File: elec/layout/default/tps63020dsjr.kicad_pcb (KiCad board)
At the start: 2 copper layers, 225.7 x 100.8 mm, 0 parts

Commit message: layout
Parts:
- added C1: Multilayer Ceramic Capacitors MLCC - SMD/SMT 10uF 10V 0805 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, lib:C0805, F.Cu at (118.5, 46.4)
- added C2: Multilayer Ceramic Capacitors MLCC - SMD/SMT 10uF 10V 0805 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, lib:C0805, F.Cu at (118.5, 44.4)
- added C3: Multilayer Ceramic Capacitors MLCC - SMD/SMT 10uF 10V 0805 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, lib:C0805, F.Cu at (118.4, 53.6)
- added C4: Multilayer Ceramic Capacitors MLCC - SMD/SMT 10uF 10V 0805 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, lib:C0805, F.Cu at (118.4, 55.6)
- added C5: Multilayer Ceramic Capacitors MLCC - SMD/SMT 100nF 10V 0402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, lib:C0402, F.Cu at (115.6, 51.1)
- added L1: , lib:IND-SMD_L2.5-W2.0_WPN252012H, F.Cu at (122.7, 49.6)
- added R1: Chip Resistor - Surface Mount 1MOhms ±5% 1/16W 0402 RoHS, lib:R0402, F.Cu at (119.1, 52.1)
- added R2: Chip Resistor - Surface Mount 180KOhms ±5% 1/16W 0402 RoHS, lib:R0402, F.Cu at (117.2, 52.1)
- added R3: Chip Resistor - Surface Mount 1MOhms ±5% 1/16W 0402 RoHS, lib:R0402, F.Cu at (115.7, 48.1)
- added U1: , lib:VSON-14_L4.0-W3.0-P0.50-BL-EP_TI_DSJ, F.Cu at (119.0, 49.5)
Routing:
- net vcc-1: track 0.00 -> 6.20 mm
- net vcc: track 0.00 -> 5.63 mm
- net l1: track 0.00 -> 2.59 mm
- net l2: track 0.00 -> 2.54 mm
- net out: track 0.00 -> 2.08 mm
- net gnd: track 0.00 -> 1.99 mm
- net vina: track 0.00 -> 1.41 mm
- net pg: track 0.00 -> 1.29 mm

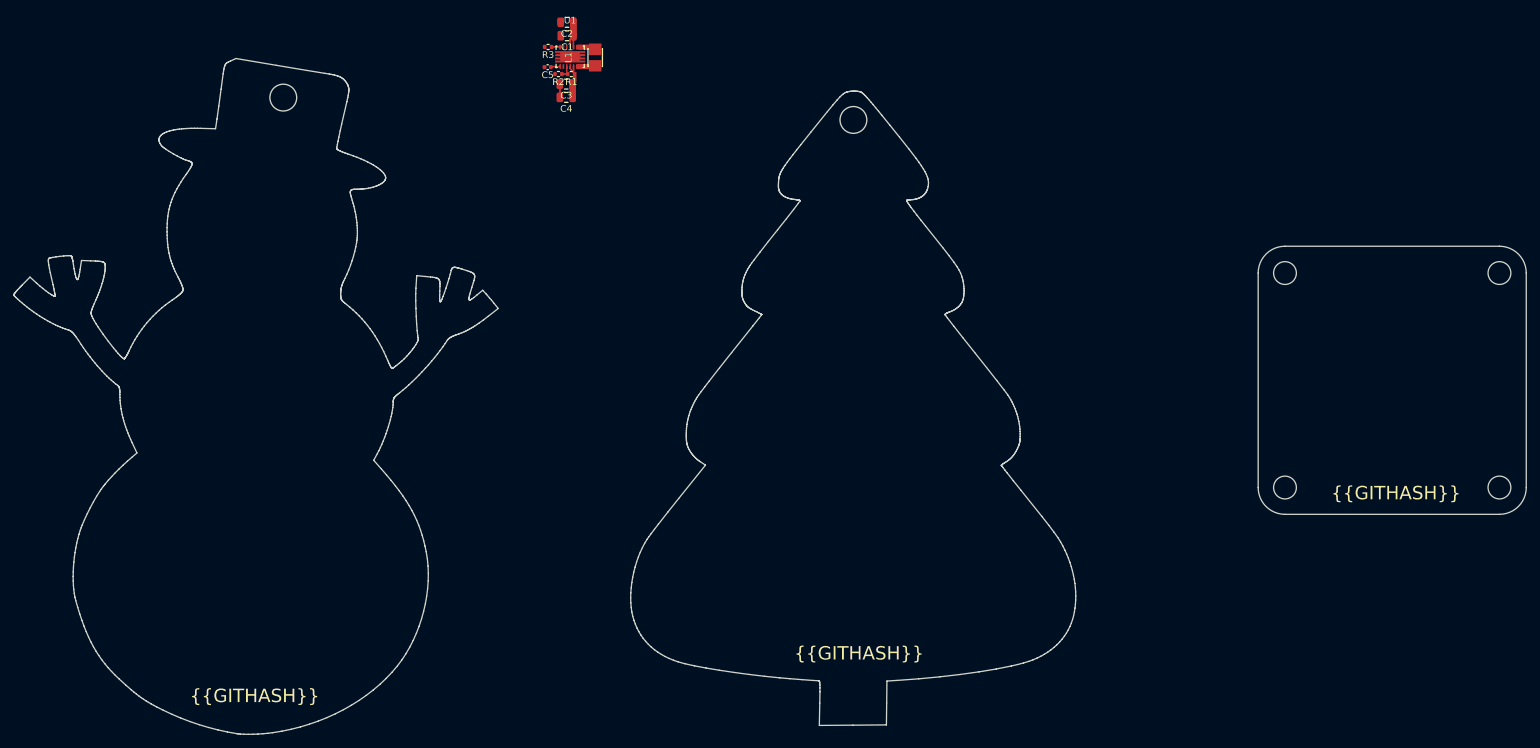
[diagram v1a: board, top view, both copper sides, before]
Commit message: update layout file to latest kicad version, remove the snowman
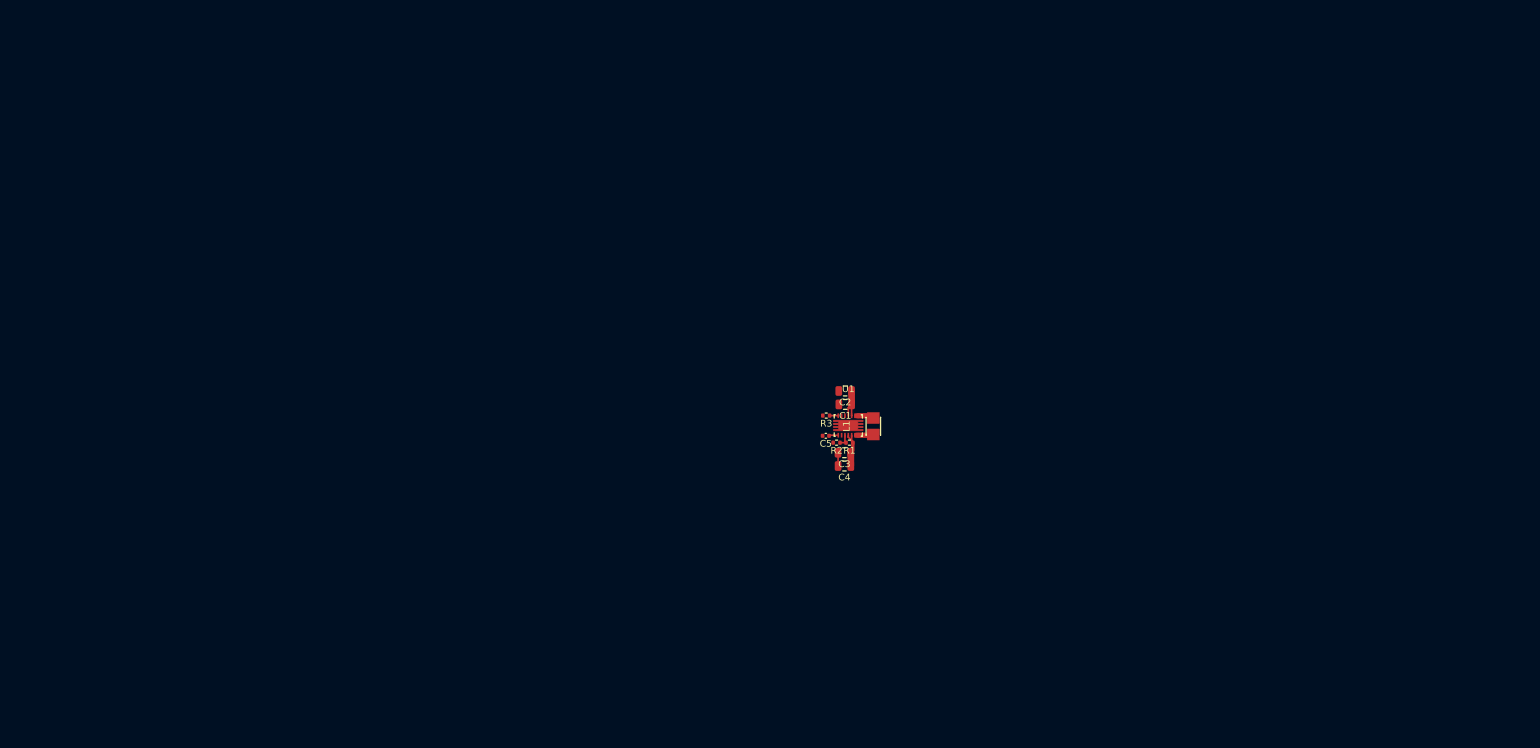
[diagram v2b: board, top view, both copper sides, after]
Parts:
- moved C3 68.9 mm to (159.9, 108.6)
- moved L1 68.9 mm to (164.2, 104.6)
- moved C1 68.9 mm to (160.0, 101.4)
- moved C2 68.9 mm to (160.0, 99.4)
- moved R1 68.9 mm to (160.6, 107.1)
- moved R2 68.9 mm to (158.7, 107.1)
- moved U1 68.9 mm to (160.5, 104.5)
- moved C4 68.9 mm to (159.9, 110.6)
- moved C5 68.9 mm to (157.1, 106.1)
- moved R3 68.9 mm to (157.2, 103.1)
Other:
- board outline removed
- board text removed: "{{GITHASH}}"

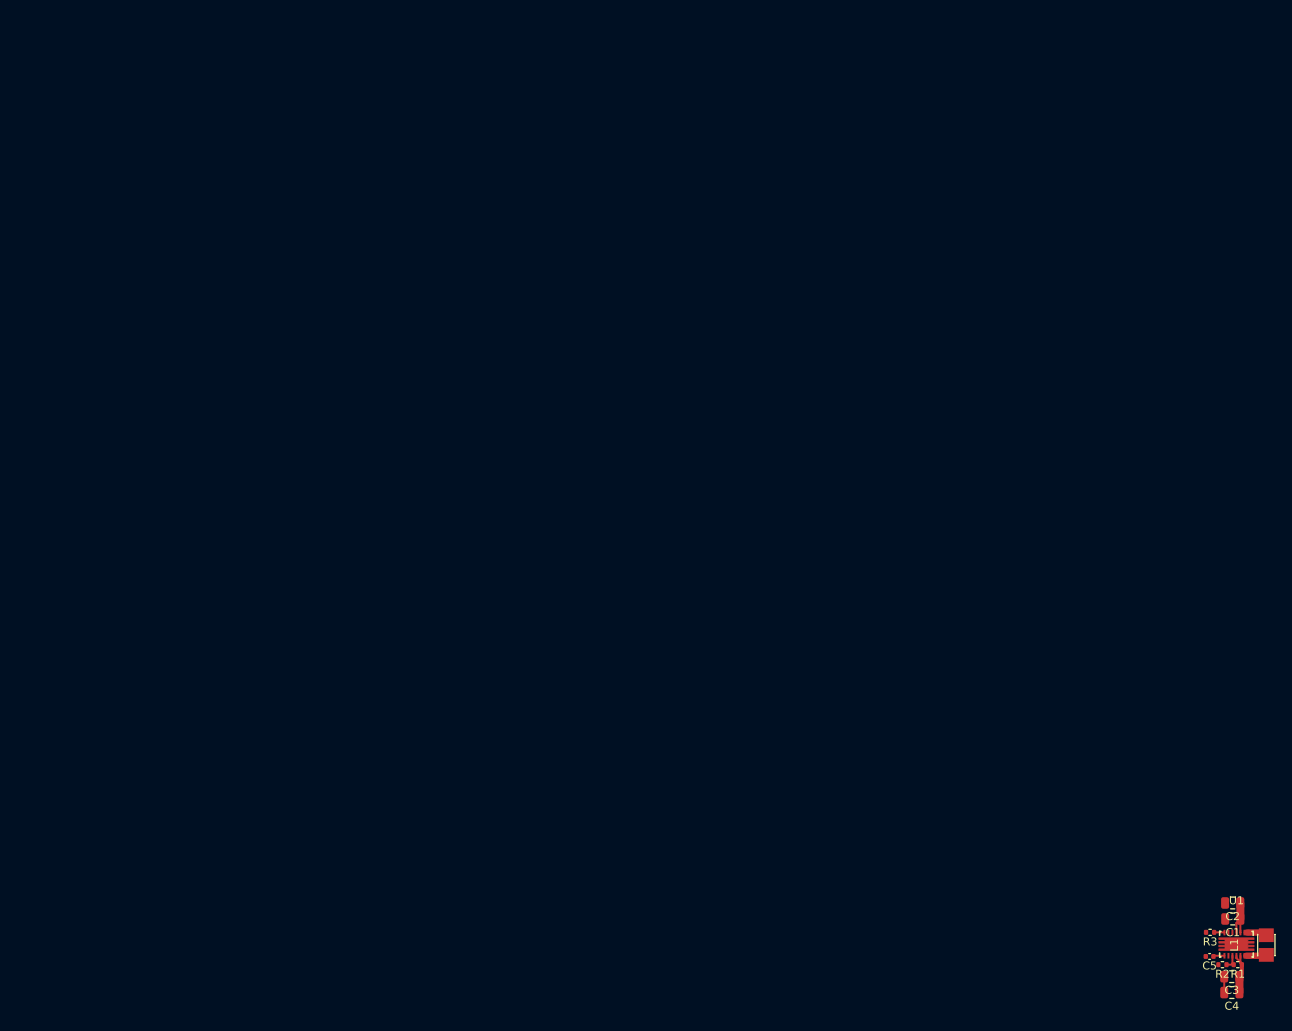
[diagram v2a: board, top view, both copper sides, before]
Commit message: Update regulator and passives to library defintions
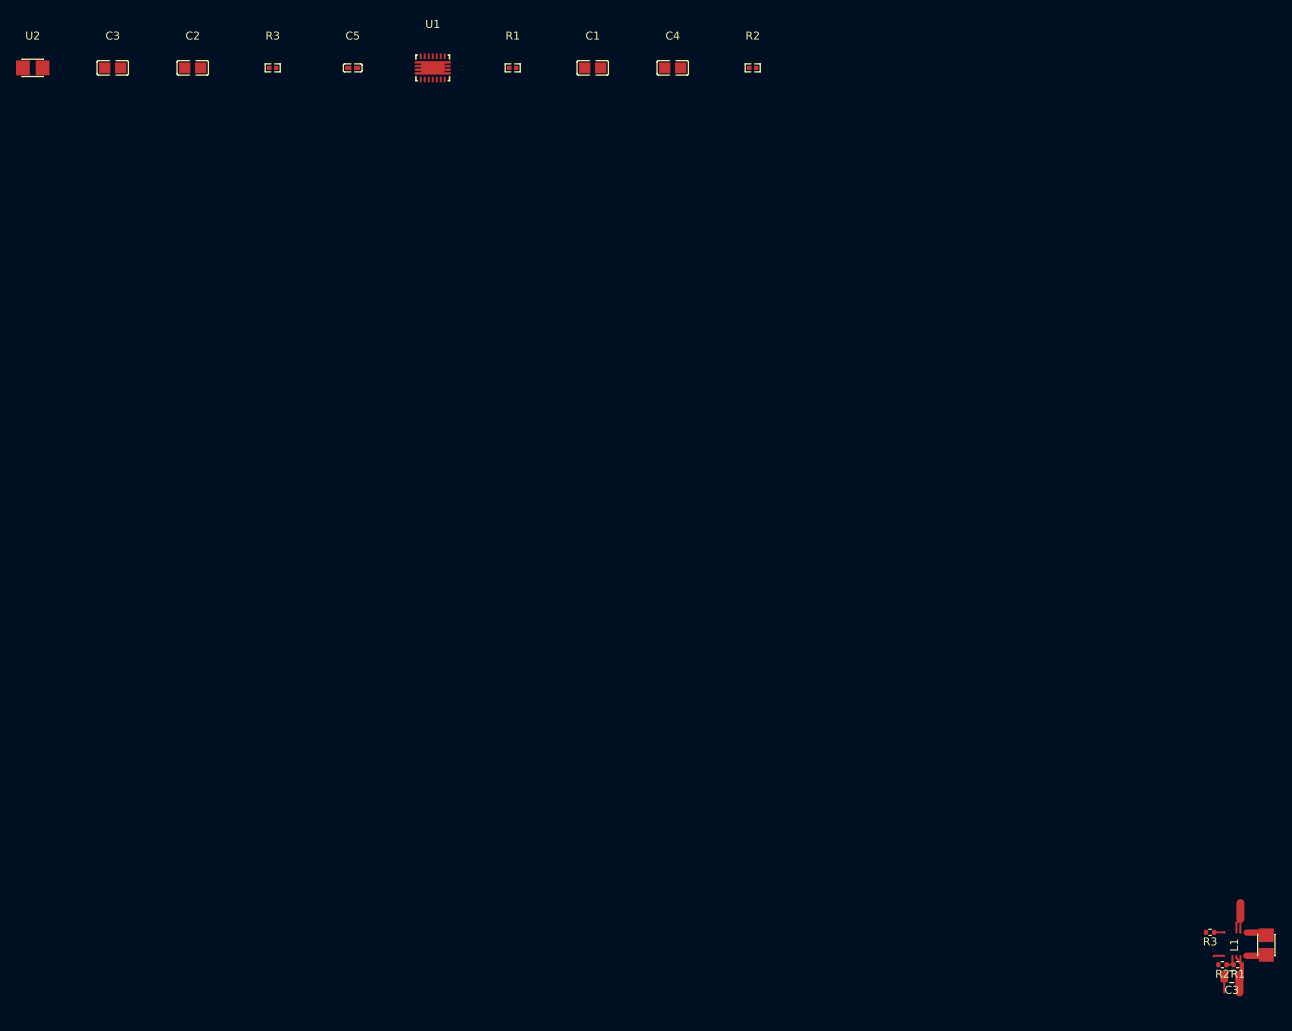
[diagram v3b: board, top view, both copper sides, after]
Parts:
- added C3: 10µF ±10% 25V X5R, atopile:C0805-3b2e55, F.Cu at (20.0, -5.00)
- added R1: 10kΩ ±1% 62.5mW, atopile:R0402-56259e, F.Cu at (70.0, -5.00)
- added R2: 26.1kΩ ±1% 62.5mW, atopile:R0402-56259e, F.Cu at (100.0, -5.00)
- added R3: 1MΩ ±1% 62.5mW, atopile:R0402-56259e, F.Cu at (40.0, -5.00)
- added U2: 1.5µH ±20%, lib:IND-SMD_L2.5-W2.0_WPN252012H, F.Cu at (10.0, -5.00)
- C1, C2, C4: value Multilayer Ceramic Capacitors MLCC - SMD/SMT 10uF 10V 0805 RoHS -> 10µF ±10% 25V X5R; footprint lib:C0805 -> atopile:C0805-3b2e55
- C5: value Multilayer Ceramic Capacitors MLCC - SMD/SMT 100nF 10V 0402 RoHS -> 100nF ±10% 16V X7R; footprint lib:C0402 -> atopile:C0402-b3ef17
- moved C2 166.7 mm to (30.0, -5.00), turned to 0 degrees
- moved C5 154.3 mm to (50.0, -5.00), turned to 0 degrees
- moved U1 148.6 mm to (60.0, -5.00)
- moved C4 135.1 mm to (90.0, -5.00), turned to 0 degrees
- moved C1 133.1 mm to (80.0, -5.00), turned to 0 degrees
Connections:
- net vcc renamed hv
- net vina renamed EN
- C4 pad 1: vcc-1 -> hv-1
- L1 pad 2: l2 -> (no net)
- R1 pad 2: out -> (no net)
- R2 pad 1: out -> (no net)
- U1 pad 14: pg -> PG
- U1 pad 3: out -> FB
- U1 pad 4: vcc-1 -> hv-1
- U1 pad 5: vcc-1 -> hv-1
- U1 pad 6: l2 -> L2
- U1 pad 7: l2 -> L2
- U1 pad 8: l1 -> L1
- U1 pad 9: l1 -> L1
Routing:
- net (no net): track 0.00 -> 11.7 mm
- net hv: track 5.63 -> 0.00 mm
- net l2: track 2.54 -> 0.00 mm
- net out: track 2.08 -> 0.00 mm
- net EN: track 1.41 -> 0.00 mm

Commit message: Relink layout
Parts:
- removed the C3 at (159.9, 108.6)
- removed the C3 at (20.0, -5.00)
- removed the R1 at (160.6, 107.1)
- removed the R1 at (70.0, -5.00)
- removed the R2 at (158.7, 107.1)
- removed the R2 at (100.0, -5.00)
- removed the R3 at (157.2, 103.1)
- removed the R3 at (40.0, -5.00)
- removed U2: 1.5µH ±20%, lib:IND-SMD_L2.5-W2.0_WPN252012H
- added C3: 10µF ±10% 25V X5R, atopile:C0805-3b2e55, F.Cu at (134.9, 99.3)
- added R1: 10kΩ ±1% 62.5mW, atopile:R0402-56259e, F.Cu at (132.5, 99.2)
- added R2: 26.1kΩ ±1% 62.5mW, atopile:R0402-56259e, F.Cu at (132.5, 101.1)
- added R3: 1MΩ ±1% 62.5mW, atopile:R0402-56259e, F.Cu at (132.4, 92.5)
- L1: value (none) -> 1.5µH ±20% 2.4A 72mΩ; footprint lib:IND-SMD_L2.5-W2.0_WPN252012H -> atopile:IND-SMD_L2.5-W2.0_WPN252012H-c19fd2
- moved C2 142.0 mm to (134.9, 90.8), turned to 180 degrees
- moved C5 130.4 mm to (131.8, 96.5), turned to 90 degrees
- moved U1 125.7 mm to (134.9, 96.0)
- moved C4 115.3 mm to (134.9, 101.2), turned to 180 degrees
- moved C1 112.0 mm to (134.9, 92.6), turned to 180 degrees
- moved L1 27.2 mm to (138.4, 96.0)
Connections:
- L1 pad 1: l1 -> L1
- L1 pad 2: (no net) -> L2
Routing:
- net (no net): track 11.7 -> 0.00 mm
- net EN: track 0.00 -> 7.15 mm, vias 0 -> 2
- net hv-1: track 0.00 -> 7.11 mm, vias 0 -> 2
- net vcc-1: track 6.20 -> 0.00 mm
- net FB: track 0.00 -> 5.14 mm, vias 0 -> 2
- net gnd: track 1.99 -> 4.97 mm
- net l1: track 2.59 -> 0.00 mm
- net PG: track 0.00 -> 1.95 mm
- net pg: track 1.29 -> 0.00 mm
- added copper zone on F.Cu, net L1
- added copper zone on F.Cu, net L2
- added copper zone on F.Cu, net gnd
- added copper zone on F.Cu, net hv
